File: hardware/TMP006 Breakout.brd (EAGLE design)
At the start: 20.3 x 20.3 mm, 14 parts, among them U1 TMP006

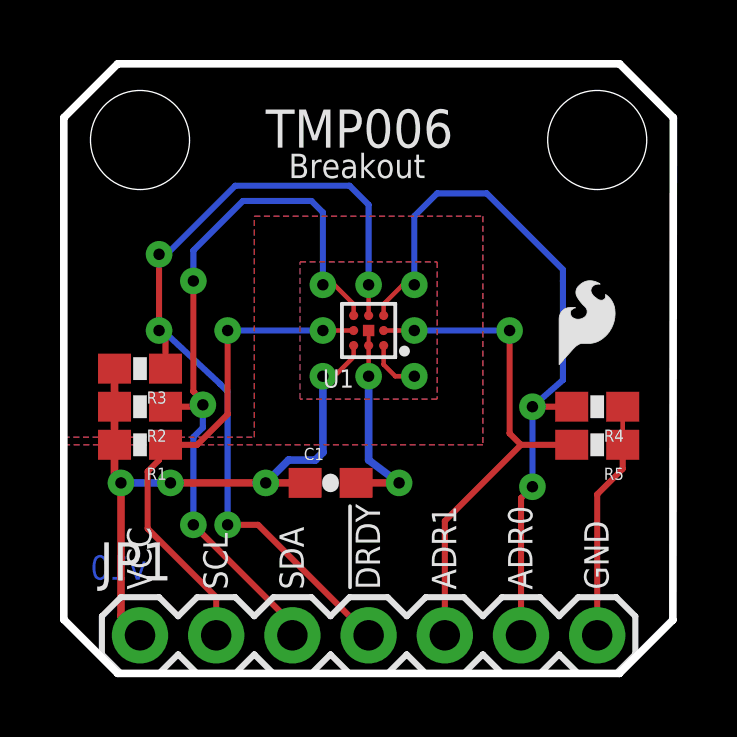
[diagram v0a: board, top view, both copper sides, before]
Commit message: Added I2C addresses on schematic, minor silk and board updates
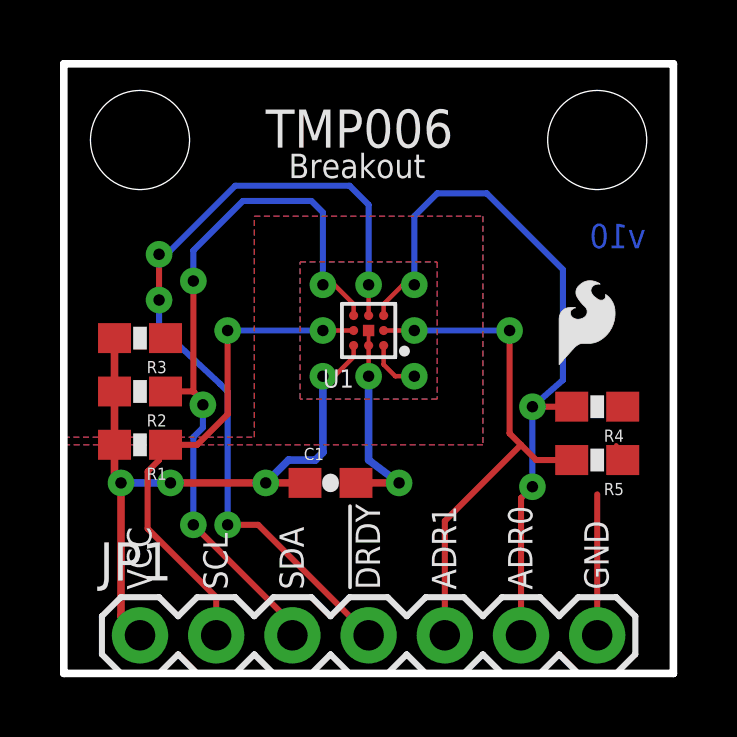
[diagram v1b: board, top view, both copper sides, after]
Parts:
- moved LOGO2 10.4 mm to (2.67, 11.3)
- moved R3 1.02 mm to (2.54, 11.2)
- moved R5 0.51 mm to (17.8, 7.11)
- moved R2 0.51 mm to (2.54, 9.40)
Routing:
- net GND: track 16.5 -> 13.9 mm
- net !DRDY: track 29.8 -> 28.1 mm
- net VCC: track 22.1 -> 23.1 mm
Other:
- outline, holes or cut-outs redrawn
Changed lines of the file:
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@@
 <board>
 <plain>
-<wire x1="0" y1="18.52395" x2="0" y2="1.79605" width="0.254" layer="20"/>
-<wire x1="0" y1="1.79605" x2="1.79605" y2="0" width="0.254" layer="20"/>
-<wire x1="1.79605" y1="0" x2="18.519790625" y2="0" width="0.254" layer="20"/>
-<wire x1="18.519790625" y1="0" x2="20.301753125" y2="1.781175" width="0.254" layer="20"/>
-<wire x1="20.301753125" y1="1.781175" x2="20.31823125" y2="18.52295" width="0.254" layer="20"/>
-<wire x1="20.31823125" y1="18.52295" x2="18.52218125" y2="20.32" width="0.254" layer="20"/>
-<wire x1="18.52218125" y1="20.32" x2="1.79605" y2="20.32" width="0.254" layer="20"/>
-<wire x1="1.79605" y1="20.32" x2="0" y2="18.52395" width="0.254" layer="20"/>
+<wire x1="0" y1="20.32" x2="0" y2="0" width="0.254" layer="20"/>
+<wire x1="0" y1="0" x2="20.32" y2="0" width="0.254" layer="20"/>
+<wire x1="20.32" y1="0" x2="20.32" y2="20.32" width="0.254" layer="20"/>
+<wire x1="20.32" y1="20.32" x2="0" y2="20.32" width="0.254" layer="20"/>
 <text x="6.731" y="17.526" size="1.27" layer="21" font="vector" ratio="15">TMP006</text>
 <text x="19.05" y="-13.97" size="1.27" layer="27" font="vector" ratio="15">Jordan McConnell</text>
@@
 <text x="12.319" y="15.367" size="0.8128" layer="22" font="vector" ratio="15" rot="MR0">Sensor</text>
 <text x="12.827" y="14.351" size="0.8128" layer="22" font="vector" ratio="15" rot="MR0">Breakout</text>
-<text x="0.889" y="3.937" size="0.8128" layer="16" font="vector" ratio="15" rot="MR180">v10</text>
+<text x="17.526" y="14.986" size="0.8128" layer="16" font="vector" ratio="15" rot="MR180">v10</text>
 <rectangle x1="10.287" y1="10.795" x2="10.541" y2="11.049" layer="41"/>
 <rectangle x1="10.795" y1="10.795" x2="11.049" y2="11.049" layer="41"/>
+<text x="17.399" y="2.794" size="0.8128" layer="22" font="vector" ratio="15" rot="MR90">GND</text>
+<text x="14.859" y="2.794" size="0.8128" layer="22" font="vector" ratio="15" rot="MR90">ADR0</text>
+<text x="12.319" y="2.794" size="0.8128" layer="22" font="vector" ratio="15" rot="MR90">ADR1</text>
+<text x="9.779" y="2.794" size="0.8128" layer="22" font="vector" ratio="15" rot="MR90">!DRDY</text>
+<text x="7.239" y="2.794" size="0.8128" layer="22" font="vector" ratio="15" rot="MR90">SDA</text>
+<text x="4.699" y="2.794" size="0.8128" layer="22" font="vector" ratio="15" rot="MR90">SCL</text>
+<text x="2.159" y="2.794" size="0.8128" layer="22" font="vector" ratio="15" rot="MR90">VCC</text>
 </plain>
 <attributes>
@@
 <element name="U1" library="SparkFun-DigitalIC" package="BGA8DS" value="TMP006" x="10.16" y="11.43"/>
 <element name="R1" library="SparkFun-Resistors" package="0603-RES" value="10k" x="2.54" y="7.62" rot="R180"/>
-<element name="R2" library="SparkFun-Resistors" package="0603-RES" value="10k" x="2.54" y="8.89" rot="R180"/>
-<element name="R3" library="SparkFun-Resistors" package="0603-RES" value="10k" x="2.54" y="10.16" rot="R180"/>
+<element name="R2" library="SparkFun-Resistors" package="0603-RES" value="10k" x="2.54" y="9.398" rot="R180"/>
+<element name="R3" library="SparkFun-Resistors" package="0603-RES" value="10k" x="2.54" y="11.176" rot="R180"/>
 <element name="R4" library="SparkFun-Resistors" package="0603-RES" value="10k" x="17.78" y="8.89" rot="R180"/>
-<element name="R5" library="SparkFun-Resistors" package="0603-RES" value="10k" x="17.78" y="7.62" rot="R180"/>
+<element name="R5" library="SparkFun-Resistors" package="0603-RES" value="10k" x="17.78" y="7.112" rot="R180"/>
 <element name="C1" library="SparkFun-Capacitors" package="0603-CAP" value="0.1uF" x="8.89" y="6.35"/>
 <element name="JP1" library="SparkFun-Connectors" package="1X07" value="" x="2.54" y="1.27"/>
 <element name="LOGO1" library="SparkFun-Aesthetics" package="SFE-LOGO-FLAME" value="LOGO-SFESK" x="16.51" y="10.287"/>
-<element name="LOGO2" library="SparkFun-Aesthetics" package="OSHW-LOGO-S" value="OSHW-LOGOS" x="10.16" y="4.064" rot="MR0"/>
+<element name="LOGO2" library="SparkFun-Aesthetics" package="OSHW-LOGO-S" value="OSHW-LOGOS" x="2.667" y="11.303" rot="MR0"/>
 <element name="STANDOFF1" library="SparkFun-Electromechanical" package="STAND-OFF" value="STAND-OFF" x="2.54" y="17.78"/>
 <element name="STANDOFF2" library="SparkFun-Electromechanical" package="STAND-OFF" value="STAND-OFF" x="17.78" y="17.78"/>
@@
 <wire x1="8.636" y1="9.906" x2="8.636" y2="7.366" width="0.254" layer="16"/>
 <wire x1="1.905" y1="7.605" x2="1.69" y2="7.62" width="0.1524" layer="1"/>
-<wire x1="1.69" y1="7.62" x2="1.69" y2="8.89" width="0.254" layer="1"/>
-<wire x1="1.69" y1="8.89" x2="1.69" y2="10.16" width="0.254" layer="1"/>
+<wire x1="1.69" y1="7.62" x2="1.69" y2="9.398" width="0.254" layer="1"/>
+<wire x1="1.69" y1="9.398" x2="1.69" y2="11.176" width="0.254" layer="1"/>
 <via x="1.905" y="6.35" extent="1-16" drill="0.381"/>
 <via x="3.556" y="6.35" extent="1-16" drill="0.381"/>
@@
 <wire x1="11.176" y1="6.35" x2="9.74" y2="6.35" width="0.254" layer="1"/>
 <wire x1="17.78" y1="1.27" x2="17.78" y2="5.969" width="0.2032" layer="1"/>
-<wire x1="18.415" y1="7.605" x2="18.63" y2="7.62" width="0.1524" layer="1"/>
-<wire x1="18.63" y1="7.62" x2="18.63" y2="8.89" width="0.1524" layer="1"/>
+<wire x1="18.415" y1="7.605" x2="18.63" y2="7.112" width="0.1524" layer="1"/>
 <polygon width="0.254" layer="1" isolate="0.3048">
 <vertex x="0" y="7.62"/>
-<vertex x="0" y="1.79605"/>
-<vertex x="1.79605" y="0"/>
-<vertex x="18.52395" y="0"/>
-<vertex x="20.32" y="1.79605"/>
-<vertex x="20.32" y="18.52395"/>
-<vertex x="18.52395" y="20.32"/>
-<vertex x="1.79605" y="20.32"/>
-<vertex x="0" y="18.52395"/>
+<vertex x="0" y="0"/>
+<vertex x="20.32" y="0"/>
+<vertex x="20.32" y="20.32"/>
+<vertex x="0" y="20.32"/>
 <vertex x="0" y="7.874"/>
 <vertex x="6.35" y="7.874"/>
@@
 <polygon width="0.254" layer="16" isolate="0.3048">
 <vertex x="0" y="7.62"/>
-<vertex x="0" y="1.79605"/>
-<vertex x="1.79605" y="0"/>
-<vertex x="18.52395" y="0"/>
-<vertex x="20.32" y="1.79605"/>
-<vertex x="20.32" y="18.52395"/>
-<vertex x="18.52395" y="20.32"/>
-<vertex x="1.79605" y="20.32"/>
-<vertex x="0" y="18.52395"/>
+<vertex x="0" y="0"/>
+<vertex x="20.32" y="0"/>
+<vertex x="20.32" y="20.32"/>
+<vertex x="0" y="20.32"/>
 <vertex x="0" y="7.874"/>
 <vertex x="6.35" y="7.874"/>
@@
 <vertex x="7.874" y="9.144"/>
 </polygon>
-<wire x1="17.78" y1="5.969" x2="18.63" y2="6.819" width="0.2032" layer="1"/>
-<wire x1="18.63" y1="6.819" x2="18.63" y2="7.62" width="0.2032" layer="1"/>
+<wire x1="18.63" y1="6.819" x2="18.63" y2="7.112" width="0.2032" layer="1"/>
 </signal>
 <signal name="SCL">
@@
 <wire x1="4.318" y1="9.398" x2="4.6355" y2="9.0805" width="0.2032" layer="1"/>
 <wire x1="4.6355" y1="9.0805" x2="4.6355" y2="8.9535" width="0.2032" layer="1"/>
-<wire x1="3.39" y1="8.89" x2="4.572" y2="8.89" width="0.2032" layer="1"/>
-<wire x1="4.572" y1="8.89" x2="4.6355" y2="8.9535" width="0.2032" layer="1"/>
+<wire x1="3.39" y1="9.398" x2="4.318" y2="9.398" width="0.2032" layer="1"/>
 </signal>
 <signal name="!DRDY">
@@
 <wire x1="10.16" y1="12.954" x2="10.16" y2="15.621" width="0.2032" layer="16"/>
 <via x="3.175" y="13.97" extent="1-16" drill="0.381"/>
-<wire x1="3.175" y1="10.175" x2="3.39" y2="10.16" width="0.1524" layer="1"/>
-<wire x1="3.175" y1="13.97" x2="3.175" y2="11.43" width="0.2032" layer="1"/>
-<via x="3.175" y="11.43" extent="1-16" drill="0.381"/>
-<wire x1="3.19" y1="11.415" x2="3.175" y2="11.43" width="0.1524" layer="1"/>
+<wire x1="3.175" y1="13.97" x2="3.175" y2="12.446" width="0.2032" layer="1"/>
+<via x="3.175" y="12.446" extent="1-16" drill="0.381"/>
 <via x="5.461" y="4.953" extent="1-16" drill="0.381"/>
 <wire x1="5.461" y1="4.953" x2="6.477" y2="4.953" width="0.2032" layer="1"/>
@@
 <wire x1="3.429" y1="13.97" x2="3.175" y2="13.97" width="0.2032" layer="16"/>
 <wire x1="5.207" y1="9.652" x2="3.302" y2="11.43" width="0.2032" layer="16"/>
-<wire x1="3.302" y1="11.43" x2="3.175" y2="11.43" width="0.1524" layer="16"/>
-<wire x1="3.19" y1="11.415" x2="3.39" y2="11.215" width="0.2032" layer="1"/>
-<wire x1="3.39" y1="11.215" x2="3.39" y2="10.16" width="0.2032" layer="1"/>
 <wire x1="5.207" y1="9.652" x2="5.461" y2="9.398" width="0.2032" layer="16"/>
 <wire x1="5.461" y1="9.398" x2="5.461" y2="4.953" width="0.2032" layer="16"/>
+<wire x1="3.302" y1="11.43" x2="3.175" y2="11.557" width="0.2032" layer="16"/>
+<wire x1="3.175" y1="11.557" x2="3.175" y2="12.446" width="0.2032" layer="16"/>
+<wire x1="3.302" y1="11.43" x2="3.39" y2="11.176" width="0" layer="19" extent="1-16"/>
 </signal>
 <signal name="ADR0">
@@
 <wire x1="14.859" y1="11.43" x2="14.859" y2="8.001" width="0.2032" layer="1"/>
 <wire x1="14.859" y1="8.001" x2="15.24" y2="7.62" width="0.2032" layer="1"/>
-<wire x1="15.24" y1="7.62" x2="16.93" y2="7.62" width="0.2032" layer="1"/>
 <wire x1="12.7" y1="1.27" x2="12.7" y2="5.08" width="0.2032" layer="1"/>
 <wire x1="12.7" y1="5.08" x2="15.24" y2="7.62" width="0.2032" layer="1"/>
+<wire x1="16.93" y1="7.112" x2="15.748" y2="7.112" width="0.2032" layer="1"/>
+<wire x1="15.748" y1="7.112" x2="15.24" y2="7.62" width="0.2032" layer="1"/>
 </signal>
 </signals>

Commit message: Production readied
created panel
added fiducials
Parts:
- added FID1, FID2: FIDUCIALUFIDUCIAL, SparkFun-Aesthetics:MICRO-FIDUCIAL
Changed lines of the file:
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@@
 <?xml version="1.0" encoding="utf-8"?>
 <!DOCTYPE eagle SYSTEM "eagle.dtd">
-<eagle version="6.2">
+<eagle version="6.4">
 <drawing>
 <settings>
@@
 <setting verticaltext="up"/>
 </settings>
-<grid distance="0.05" unitdist="inch" unit="inch" style="lines" multiple="1" display="yes" altdistance="0.005" altunitdist="inch" altunit="inch"/>
+<grid distance="0.05" unitdist="inch" unit="inch" style="lines" multiple="1" display="yes" altdistance="0.01" altunitdist="inch" altunit="inch"/>
 <layers>
 <layer number="1" name="Top" color="4" fill="1" visible="yes" active="yes"/>
-<layer number="2" name="Route2" color="1" fill="3" visible="no" active="yes"/>
-<layer number="15" name="Route15" color="4" fill="6" visible="no" active="yes"/>
+<layer number="2" name="Route2" color="1" fill="3" visible="yes" active="yes"/>
+<layer number="15" name="Route15" color="4" fill="6" visible="yes" active="yes"/>
 <layer number="16" name="Bottom" color="1" fill="1" visible="yes" active="yes"/>
 <layer number="17" name="Pads" color="2" fill="1" visible="yes" active="yes"/>
 <layer number="18" name="Vias" color="2" fill="1" visible="yes" active="yes"/>
 <layer number="19" name="Unrouted" color="6" fill="1" visible="yes" active="yes"/>
-<layer number="20" name="Dimension" color="15" fill="1" visible="yes" active="yes"/>
-<layer number="21" name="tPlace" color="16" fill="1" visible="yes" active="yes"/>
-<layer number="22" name="bPlace" color="14" fill="1" visible="yes" active="yes"/>
+<layer number="20" name="Dimension" color="6" fill="1" visible="yes" active="yes"/>
+<layer number="21" name="tPlace" color="6" fill="1" visible="yes" active="yes"/>
+<layer number="22" name="bPlace" color="6" fill="1" visible="yes" active="yes"/>
 <layer number="23" name="tOrigins" color="15" fill="1" visible="yes" active="yes"/>
 <layer number="24" name="bOrigins" color="15" fill="1" visible="yes" active="yes"/>
-<layer number="25" name="tNames" color="7" fill="1" visible="no" active="yes"/>
-<layer number="26" name="bNames" color="7" fill="1" visible="no" active="yes"/>
-<layer number="27" name="tValues" color="7" fill="1" visible="no" active="yes"/>
-<layer number="28" name="bValues" color="7" fill="1" visible="no" active="yes"/>
-<layer number="29" name="tStop" color="7" fill="3" visible="no" active="yes"/>
-<layer number="30" name="bStop" color="7" fill="6" visible="no" active="yes"/>
-<layer number="31" name="tCream" color="7" fill="4" visible="no" active="yes"/>
-<layer number="32" name="bCream" color="7" fill="5" visible="no" active="yes"/>
-<layer number="39" name="tKeepout" color="4" fill="11" visible="no" active="yes"/>
-<layer number="40" name="bKeepout" color="1" fill="11" visible="no" active="yes"/>
-<layer number="41" name="tRestrict" color="4" fill="10" visible="no" active="yes"/>
-<layer number="42" name="bRestrict" color="1" fill="10" visible="no" active="yes"/>
-<layer number="44" name="Drills" color="7" fill="1" visible="no" active="yes"/>
+<layer number="25" name="tNames" color="7" fill="1" visible="yes" active="yes"/>
+<layer number="26" name="bNames" color="7" fill="1" visible="yes" active="yes"/>
+<layer number="27" name="tValues" color="7" fill="1" visible="yes" active="yes"/>
+<layer number="28" name="bValues" color="7" fill="1" visible="yes" active="yes"/>
+<layer number="29" name="tStop" color="7" fill="3" visible="yes" active="yes"/>
+<layer number="30" name="bStop" color="7" fill="6" visible="yes" active="yes"/>
+<layer number="31" name="tCream" color="7" fill="4" visible="yes" active="yes"/>
+<layer number="32" name="bCream" color="7" fill="5" visible="yes" active="yes"/>
+<layer number="39" name="tKeepout" color="4" fill="11" visible="yes" active="yes"/>
+<layer number="40" name="bKeepout" color="1" fill="11" visible="yes" active="yes"/>
+<layer number="41" name="tRestrict" color="4" fill="10" visible="yes" active="yes"/>
+<layer number="42" name="bRestrict" color="1" fill="10" visible="yes" active="yes"/>
+<layer number="44" name="Drills" color="7" fill="1" visible="yes" active="yes"/>
 <layer number="45" name="Holes" color="7" fill="1" visible="yes" active="yes"/>
-<layer number="46" name="Milling" color="3" fill="1" visible="no" active="yes"/>
+<layer number="46" name="Milling" color="3" fill="1" visible="yes" active="yes"/>
 <layer number="51" name="tDocu" color="6" fill="1" visible="yes" active="yes"/>
-<layer number="52" name="bDocu" color="7" fill="1" visible="no" active="yes"/>
+<layer number="52" name="bDocu" color="7" fill="1" visible="yes" active="yes"/>
 <layer number="3" name="Route3" color="4" fill="3" visible="no" active="no"/>
 <layer number="4" name="Route4" color="1" fill="4" visible="no" active="no"/>
@@
 </class>
 </classes>
-<designrules>
+<designrules name="default">
 <description language="en">&lt;b&gt;EAGLE Design Rules&lt;/b&gt;
 &lt;p&gt;
@@
 <element name="STANDOFF2" library="SparkFun-Electromechanical" package="STAND-OFF" value="STAND-OFF" x="17.78" y="17.78"/>
 <element name="LOGO3" library="SparkFun-Aesthetics" package="SFE-NEW-WEBLOGO" value="LOGO-SFENEW" x="19.685" y="6.223" rot="MR0"/>
+<element name="FID1" library="SparkFun-Aesthetics" package="MICRO-FIDUCIAL" value="FIDUCIALUFIDUCIAL" x="19.304" y="3.302"/>
+<element name="FID2" library="SparkFun-Aesthetics" package="MICRO-FIDUCIAL" value="FIDUCIALUFIDUCIAL" x="0.762" y="19.558"/>
 </elements>
 <signals>
